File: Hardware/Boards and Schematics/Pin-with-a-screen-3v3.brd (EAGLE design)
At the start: 54.5 x 35.2 mm, 29 parts, among them J1 AVR_SPI_PRG_6NS, Q1 MMBT2222A, Q2 BL8530, U1 ATMEGA328P, U2 MICRO-SD-SOCKET-SMD1:1, Y1 8MHz

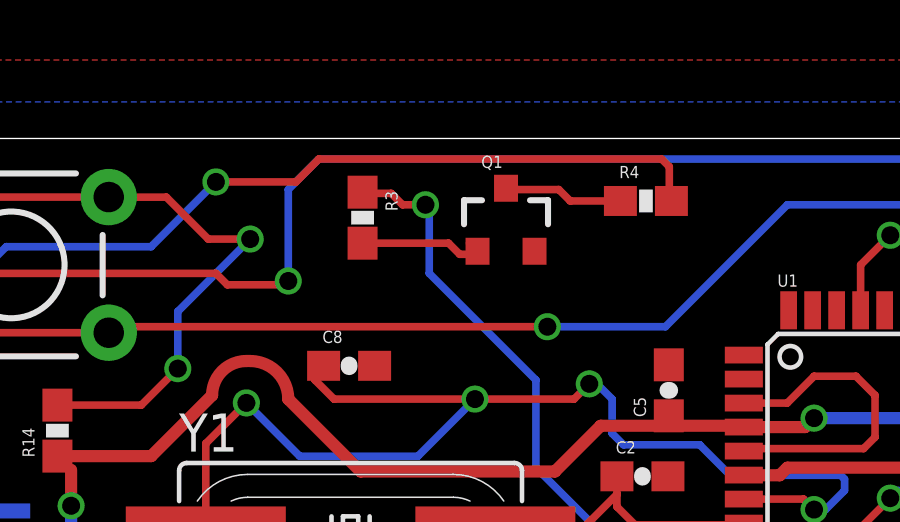
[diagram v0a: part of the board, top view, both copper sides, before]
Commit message: Removed transistor-resistor logic level shifter
Logic level shifter was used for PWM-ing backlight signal for screen.
Since MCU operates on 3v3 logic like screen, level shifter is not
necessary.
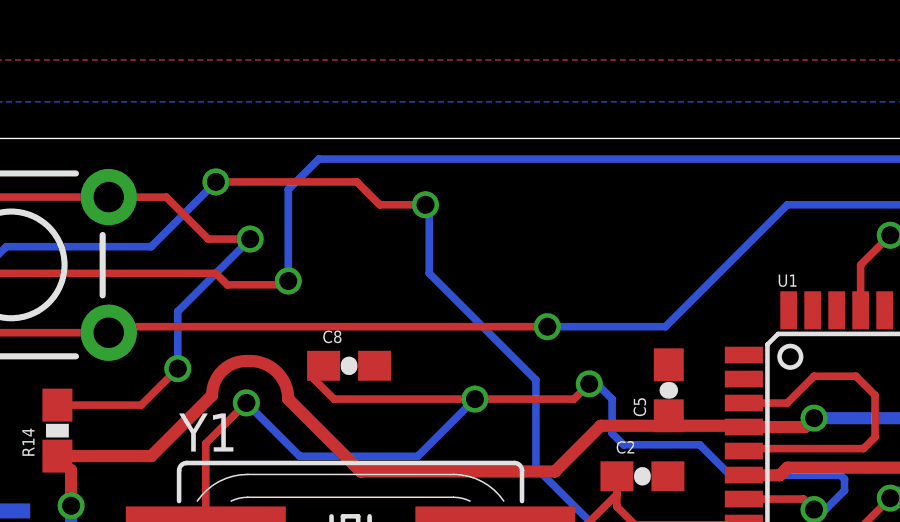
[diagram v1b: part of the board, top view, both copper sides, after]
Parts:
- removed Q1: MMBT2222A, SparkFun-DiscreteSemi:SOT23-3
- removed R3: 1k, SparkFun-Passives:0603-RES
- removed R4: 22R, SparkFun-Passives:0603-RES
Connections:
- removed net LEDK: LCD2.3, R4.2
- removed net TRAN_BASE: Q1.1, R3.2
- removed net TRAN_COLLECTOR: Q1.3, R4.1
- net GND: no longer Q1.2
- net TFT_BACKLIGHT: now also LCD2.3; no longer R3.1
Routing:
- net LEDK: track 39.3 -> 0.00 mm, vias 1 -> 0
- net TFT_BACKLIGHT: track 25.0 -> 52.6 mm, vias 2 -> 3
- net TRAN_BASE: track 4.41 -> 0.00 mm
- net TRAN_COLLECTOR: track 4.29 -> 0.00 mm
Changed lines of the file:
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@@
 <layer number="21" name="tPlace" color="7" fill="1" visible="yes" active="yes"/>
 <layer number="22" name="bPlace" color="7" fill="1" visible="yes" active="yes"/>
-<layer number="23" name="tOrigins" color="15" fill="1" visible="no" active="yes"/>
-<layer number="24" name="bOrigins" color="15" fill="1" visible="no" active="yes"/>
-<layer number="25" name="tNames" color="7" fill="1" visible="no" active="yes"/>
-<layer number="26" name="bNames" color="7" fill="1" visible="no" active="yes"/>
-<layer number="27" name="tValues" color="7" fill="1" visible="no" active="yes"/>
-<layer number="28" name="bValues" color="7" fill="1" visible="no" active="yes"/>
+<layer number="23" name="tOrigins" color="15" fill="1" visible="yes" active="yes"/>
+<layer number="24" name="bOrigins" color="15" fill="1" visible="yes" active="yes"/>
+<layer number="25" name="tNames" color="7" fill="1" visible="yes" active="yes"/>
+<layer number="26" name="bNames" color="7" fill="1" visible="yes" active="yes"/>
+<layer number="27" name="tValues" color="7" fill="1" visible="yes" active="yes"/>
+<layer number="28" name="bValues" color="7" fill="1" visible="yes" active="yes"/>
 <layer number="29" name="tStop" color="7" fill="3" visible="no" active="yes"/>
 <layer number="30" name="bStop" color="7" fill="6" visible="no" active="yes"/>
@@
 <layer number="37" name="tTest" color="7" fill="1" visible="no" active="yes"/>
 <layer number="38" name="bTest" color="7" fill="1" visible="no" active="yes"/>
-<layer number="39" name="tKeepout" color="4" fill="11" visible="no" active="yes"/>
-<layer number="40" name="bKeepout" color="1" fill="11" visible="no" active="yes"/>
-<layer number="41" name="tRestrict" color="4" fill="10" visible="no" active="yes"/>
-<layer number="42" name="bRestrict" color="1" fill="10" visible="no" active="yes"/>
-<layer number="43" name="vRestrict" color="2" fill="10" visible="no" active="yes"/>
+<layer number="39" name="tKeepout" color="4" fill="11" visible="yes" active="yes"/>
+<layer number="40" name="bKeepout" color="1" fill="11" visible="yes" active="yes"/>
+<layer number="41" name="tRestrict" color="4" fill="10" visible="yes" active="yes"/>
+<layer number="42" name="bRestrict" color="1" fill="10" visible="yes" active="yes"/>
+<layer number="43" name="vRestrict" color="2" fill="10" visible="yes" active="yes"/>
 <layer number="44" name="Drills" color="7" fill="1" visible="yes" active="yes"/>
-<layer number="45" name="Holes" color="7" fill="1" visible="no" active="yes"/>
-<layer number="46" name="Milling" color="3" fill="1" visible="no" active="yes"/>
+<layer number="45" name="Holes" color="7" fill="1" visible="yes" active="yes"/>
+<layer number="46" name="Milling" color="3" fill="1" visible="yes" active="yes"/>
 <layer number="47" name="Measures" color="7" fill="1" visible="no" active="yes"/>
 <layer number="48" name="Document" color="7" fill="1" visible="no" active="yes"/>
@@
 <element name="C4" library="SparkFun" package="0603-CAP" value="0.1uF" x="10.984" y="16.902" rot="R90"/>
 <element name="LCD2" library="adafruit" package="JD-T1800" value="JD-T1800" x="28.389" y="17.616" rot="MR90"/>
-<element name="Q1" library="SparkFun-DiscreteSemi" package="SOT23-3" value="MMBT2222A" x="32.15" y="32.47">
-<attribute name="PROD_ID" value="TRANS-08049" x="32.15" y="32.47" size="1.778" layer="27" display="off"/>
-</element>
-<element name="R3" library="SparkFun-Passives" package="0603-RES" value="1k" x="27.368" y="32.59" rot="R270"/>
-<element name="R4" library="SparkFun-Passives" package="0603-RES" value="22R" x="36.813" y="33.147"/>
 <element name="U1" library="SparkFun-DigitalIC" package="TQFP32-08" value="ATMEGA328P" x="44.37" y="25.21">
 <attribute name="PROD_ID" value="IC-09069" x="44.37" y="25.21" size="1.778" layer="27" display="off"/>
@@
 <signals>
 <signal name="GND">
-<contactref element="Q1" pad="2"/>
 <contactref element="C3" pad="2"/>
 <contactref element="U1" pad="21"/>
@@
 <wire x1="23.622" y1="27.813" x2="23.495" y2="27.813" width="0.4064" layer="1"/>
 </signal>
-<signal name="TRAN_COLLECTOR">
-<contactref element="R4" pad="1"/>
-<contactref element="Q1" pad="3"/>
-<wire x1="32.15" y1="33.57" x2="32.362" y2="33.782" width="0.254" layer="1"/>
-<wire x1="35.963" y1="33.147" x2="34.29" y2="33.147" width="0.254" layer="1"/>
-<wire x1="34.29" y1="33.147" x2="33.909" y2="33.528" width="0.254" layer="1"/>
-<wire x1="33.909" y1="33.528" x2="32.192" y2="33.528" width="0.254" layer="1"/>
-<wire x1="32.192" y1="33.528" x2="32.15" y2="33.57" width="0.254" layer="1"/>
-</signal>
-<signal name="TRAN_BASE">
-<contactref element="R3" pad="2"/>
-<contactref element="Q1" pad="1"/>
-<wire x1="30.93" y1="31.74" x2="31.2" y2="31.47" width="0.254" layer="1"/>
-<wire x1="27.368" y1="31.74" x2="30.236" y2="31.74" width="0.254" layer="1"/>
-<wire x1="30.236" y1="31.74" x2="30.607" y2="31.369" width="0.254" layer="1"/>
-<wire x1="30.607" y1="31.369" x2="31.099" y2="31.369" width="0.254" layer="1"/>
-<wire x1="31.099" y1="31.369" x2="31.2" y2="31.47" width="0.254" layer="1"/>
-</signal>
 <signal name="N$3">
 <contactref element="U1" pad="20"/>
@@
 <signal name="TFT_BACKLIGHT">
 <contactref element="U1" pad="10"/>
-<contactref element="R3" pad="1"/>
 <wire x1="42.37" y1="20.9174" x2="42.37" y2="19.637" width="0.254" layer="1"/>
 <wire x1="42.37" y1="19.637" x2="42.291" y2="19.558" width="0.254" layer="1"/>
@@
 <wire x1="29.591" y1="32.893" x2="29.464" y2="33.02" width="0.254" layer="16"/>
 <via x="29.464" y="33.02" extent="1-16" drill="0.6"/>
-<wire x1="29.464" y1="33.02" x2="28.702" y2="33.02" width="0.254" layer="1"/>
-<wire x1="28.702" y1="33.02" x2="28.321" y2="33.401" width="0.254" layer="1"/>
-<wire x1="28.321" y1="33.401" x2="27.407" y2="33.401" width="0.254" layer="1"/>
-<wire x1="27.407" y1="33.401" x2="27.368" y2="33.44" width="0.254" layer="1"/>
 <wire x1="36.957" y1="20.447" x2="38.227" y2="20.447" width="0.254" layer="1"/>
 <wire x1="38.227" y1="20.447" x2="39.116" y2="19.558" width="0.254" layer="1"/>
 <wire x1="33.147" y1="24.257" x2="36.957" y2="20.447" width="0.254" layer="16"/>
-</signal>
-<signal name="LEDK">
 <contactref element="LCD2" pad="3"/>
-<contactref element="R4" pad="2"/>
 <wire x1="15.289" y1="21.216" x2="15.282" y2="21.209" width="0.254" layer="16"/>
 <wire x1="15.282" y1="21.209" x2="12.791" y2="21.209" width="0.254" layer="16"/>
@@
 <wire x1="20.32" y1="31.623" x2="22.479" y2="33.782" width="0.254" layer="16"/>
 <via x="22.479" y="33.782" extent="1-16" drill="0.6"/>
-<wire x1="22.479" y1="33.782" x2="25.146" y2="33.782" width="0.254" layer="1"/>
-<wire x1="25.146" y1="33.782" x2="25.908" y2="34.544" width="0.254" layer="1"/>
-<wire x1="25.908" y1="34.544" x2="37.338" y2="34.544" width="0.254" layer="1"/>
-<wire x1="37.338" y1="34.544" x2="37.592" y2="34.29" width="0.254" layer="1"/>
-<wire x1="37.592" y1="34.29" x2="37.592" y2="33.218" width="0.254" layer="1"/>
-<wire x1="37.592" y1="33.218" x2="37.663" y2="33.147" width="0.254" layer="1"/>
+<wire x1="22.479" y1="33.782" x2="27.178" y2="33.782" width="0.254" layer="1"/>
 <wire x1="20.32" y1="31.623" x2="15.492" y2="31.623" width="0.254" layer="16"/>
 <wire x1="15.492" y1="31.623" x2="15" y2="31.131" width="0.254" layer="16"/>
+<wire x1="27.178" y1="33.782" x2="27.94" y2="33.02" width="0.254" layer="1"/>
+<wire x1="27.94" y1="33.02" x2="29.464" y2="33.02" width="0.254" layer="1"/>
 </signal>
 <signal name="TFTRESET">

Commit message: Changed led to red and series resistor to 51R
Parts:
- BLINKY: value Green -> Red
- R1: value 5R -> 51R
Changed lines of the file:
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@@
 <attribute name="NAME" x="35.958" y="12.524" size="0.6096" layer="25" rot="R90"/>
 </element>
-<element name="R1" library="SparkFun-Passives" package="0603-RES" value="5R" x="51.943" y="21.082" rot="R270"/>
-<element name="BLINKY" library="SparkFun" package="LED-0603" value="Green" x="51.943" y="16.383" rot="R180"/>
+<element name="R1" library="SparkFun-Passives" package="0603-RES" value="51R" x="51.943" y="21.082" rot="R270"/>
+<element name="BLINKY" library="SparkFun" package="LED-0603" value="Red" x="51.943" y="16.383" rot="R180"/>
 <element name="PAD1" library="wirepad" package="2,15/1,0" value="" x="25.3" y="17.581" smashed="yes">
 <attribute name="VALUE" x="25.3" y="18.581" size="0.0254" layer="27"/>

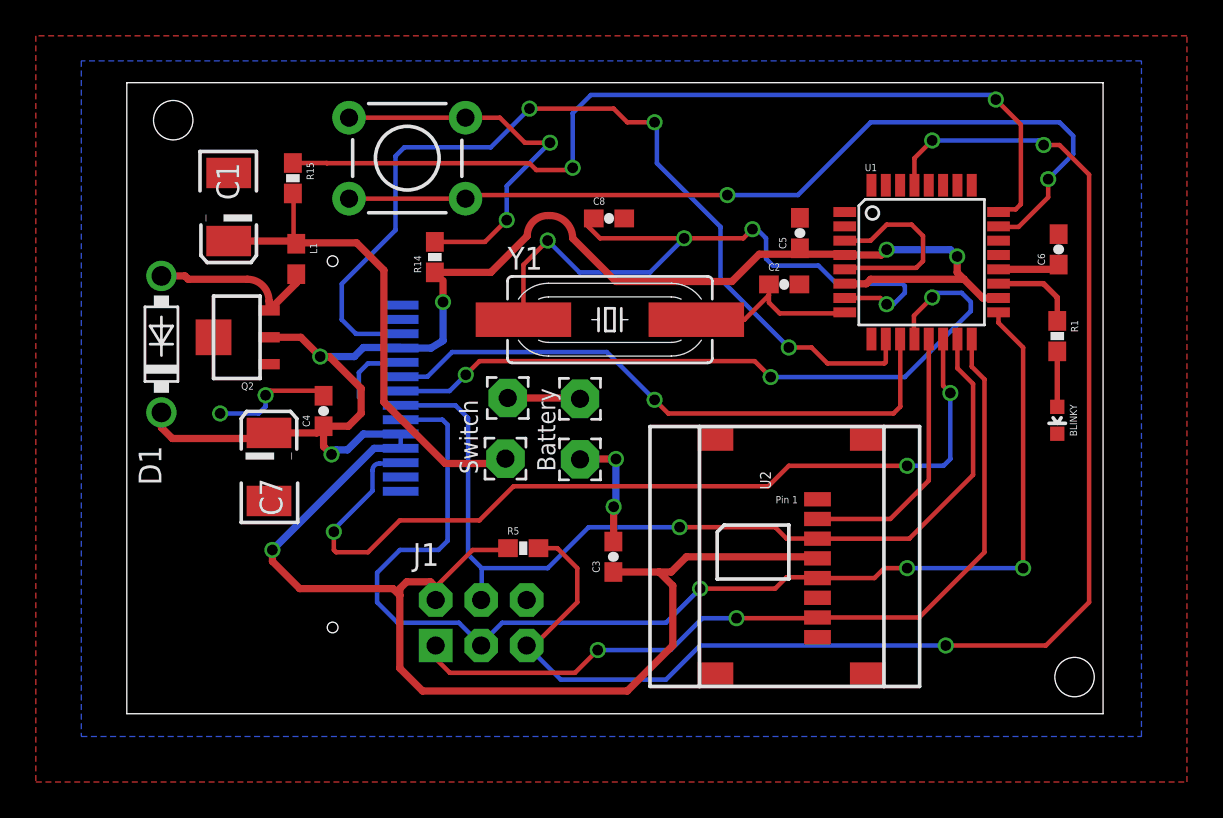
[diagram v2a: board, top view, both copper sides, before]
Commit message: Added protoboard section
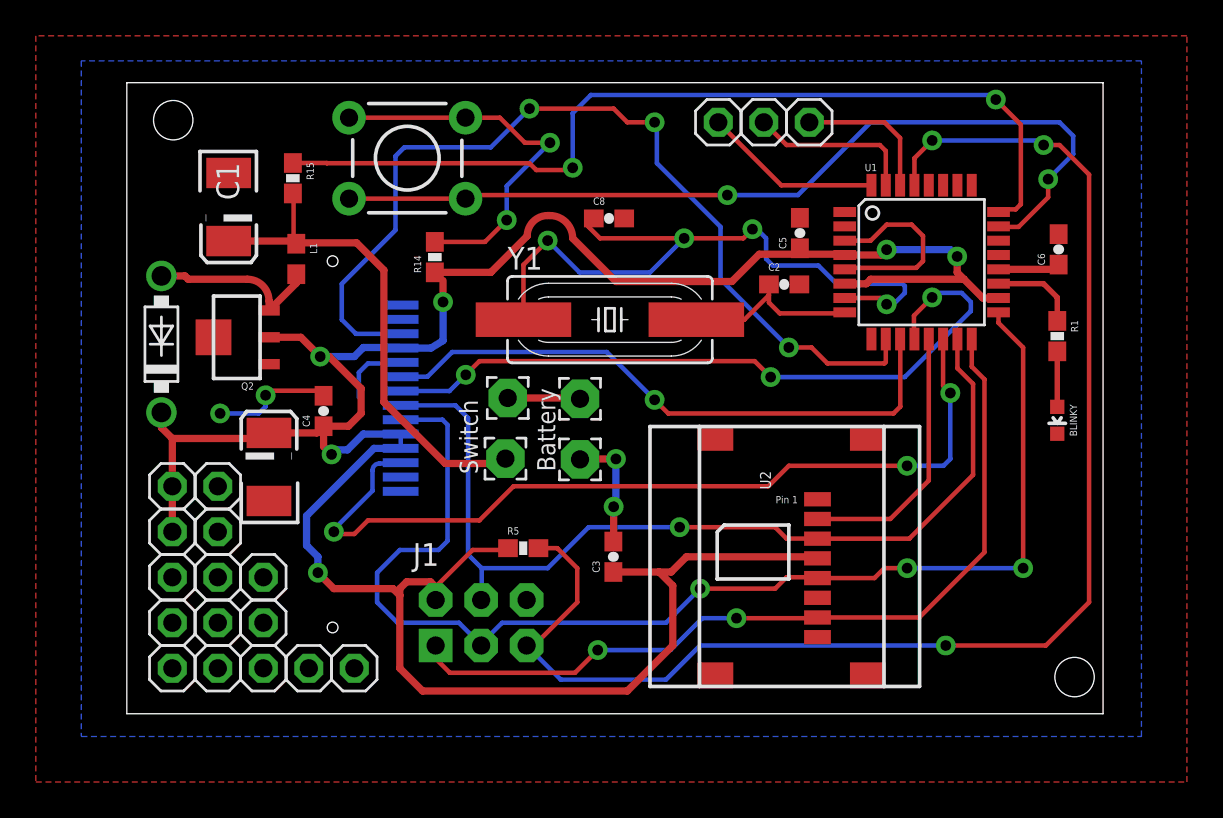
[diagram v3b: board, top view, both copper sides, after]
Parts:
- added JP1, JP10, JP11, JP12, JP13, JP14, JP15, JP16, JP17, JP18, JP19, JP2, JP3, JP5, JP6, JP7, JP8, JP9: (no value), pinhead:1X01
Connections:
- new net PD0: JP1.1, U1.30
- new net PD1: JP2.1, U1.31
- new net PD2: JP3.1, U1.32
- net 3.3V: now also JP5.1, JP7.1
- net GND: now also JP6.1, JP8.1
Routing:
- net PD2: track 0.00 -> 10.0 mm
- net PD1: track 0.00 -> 9.39 mm
- net PD0: track 0.00 -> 8.07 mm
- net 3.3V: track 146.1 -> 148.6 mm
- net TFTCS: track 50.6 -> 49.2 mm
